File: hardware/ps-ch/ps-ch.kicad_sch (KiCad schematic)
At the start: 70 parts, among them Q11 MMBT3904, U10 ADuM1401xRW, U11 LMR51610X, U13 ADuM1401xRW, U3 LM61495, U5 OPA992IDBVR

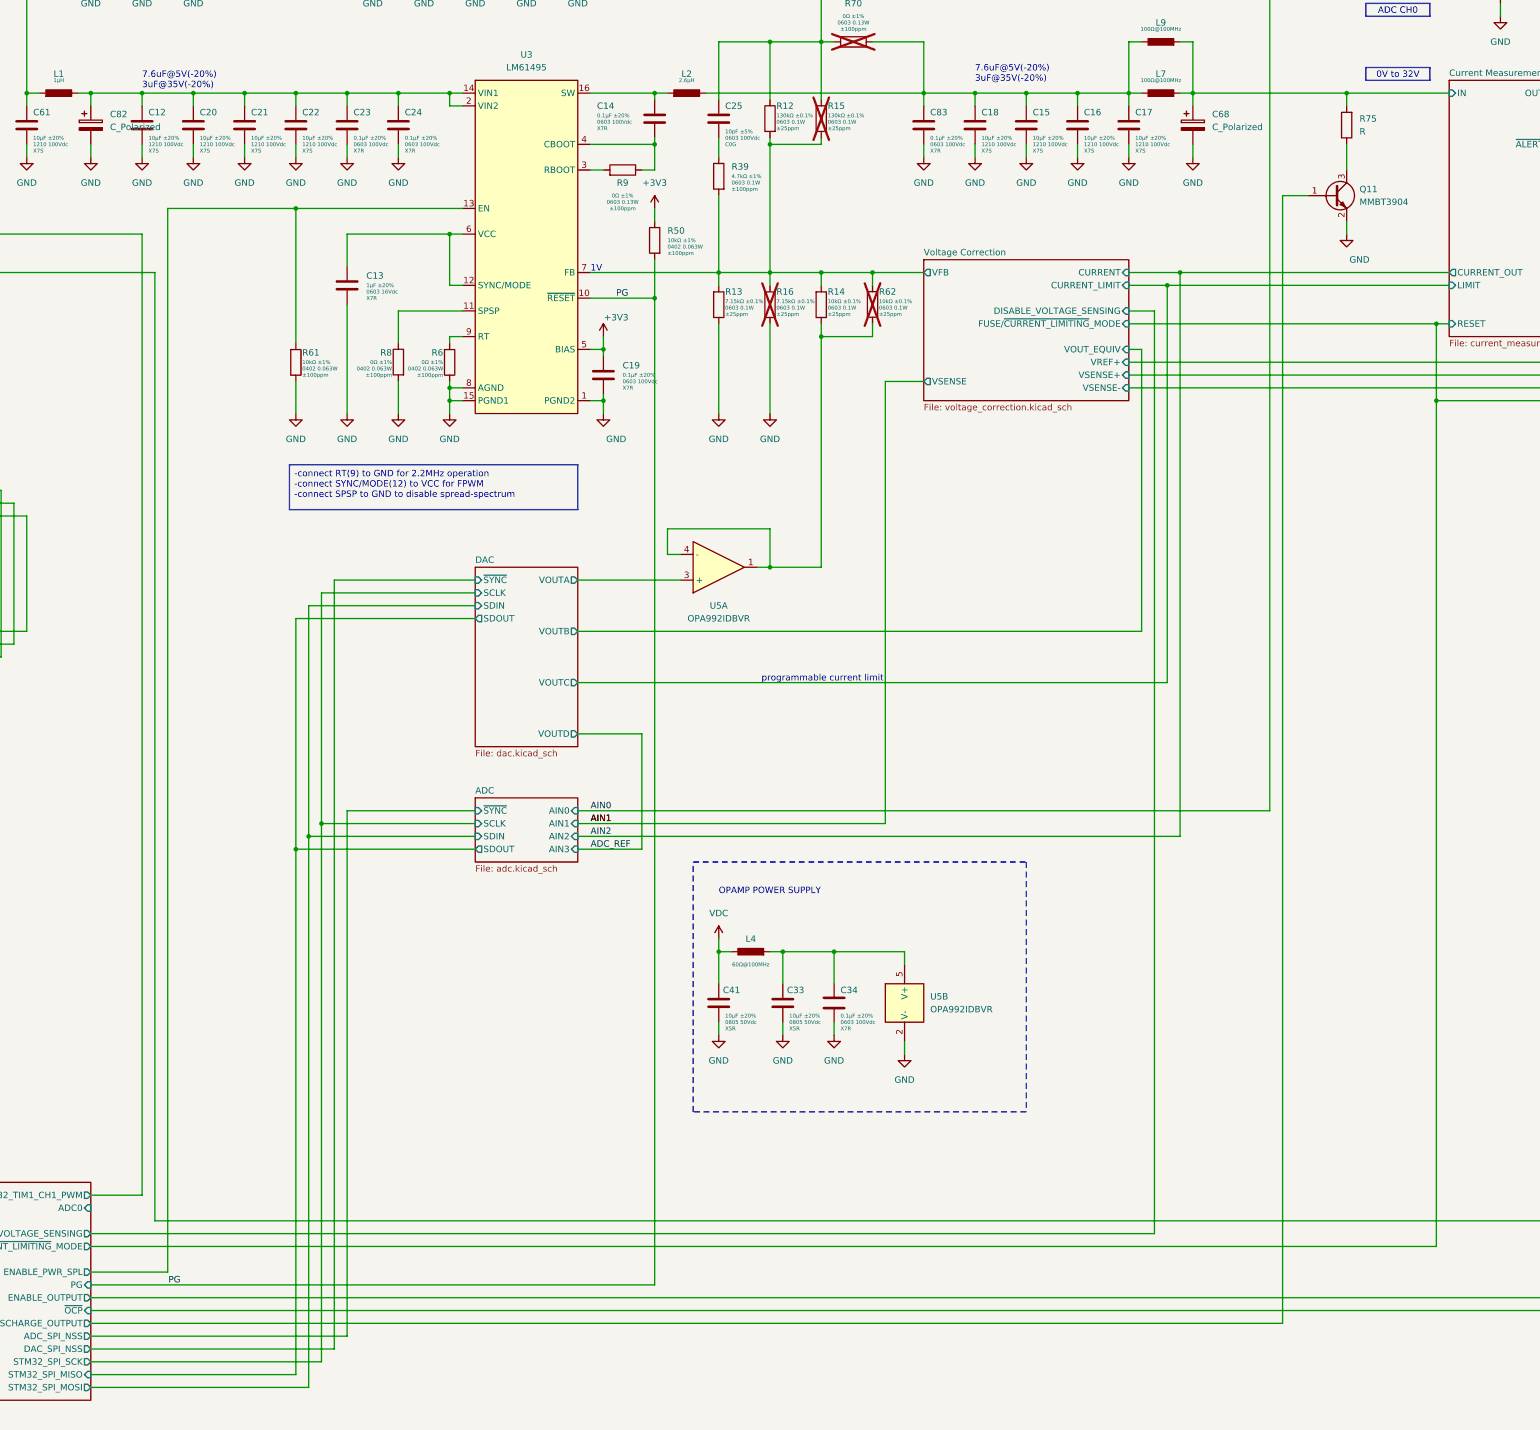
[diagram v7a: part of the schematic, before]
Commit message: added discharge resistors
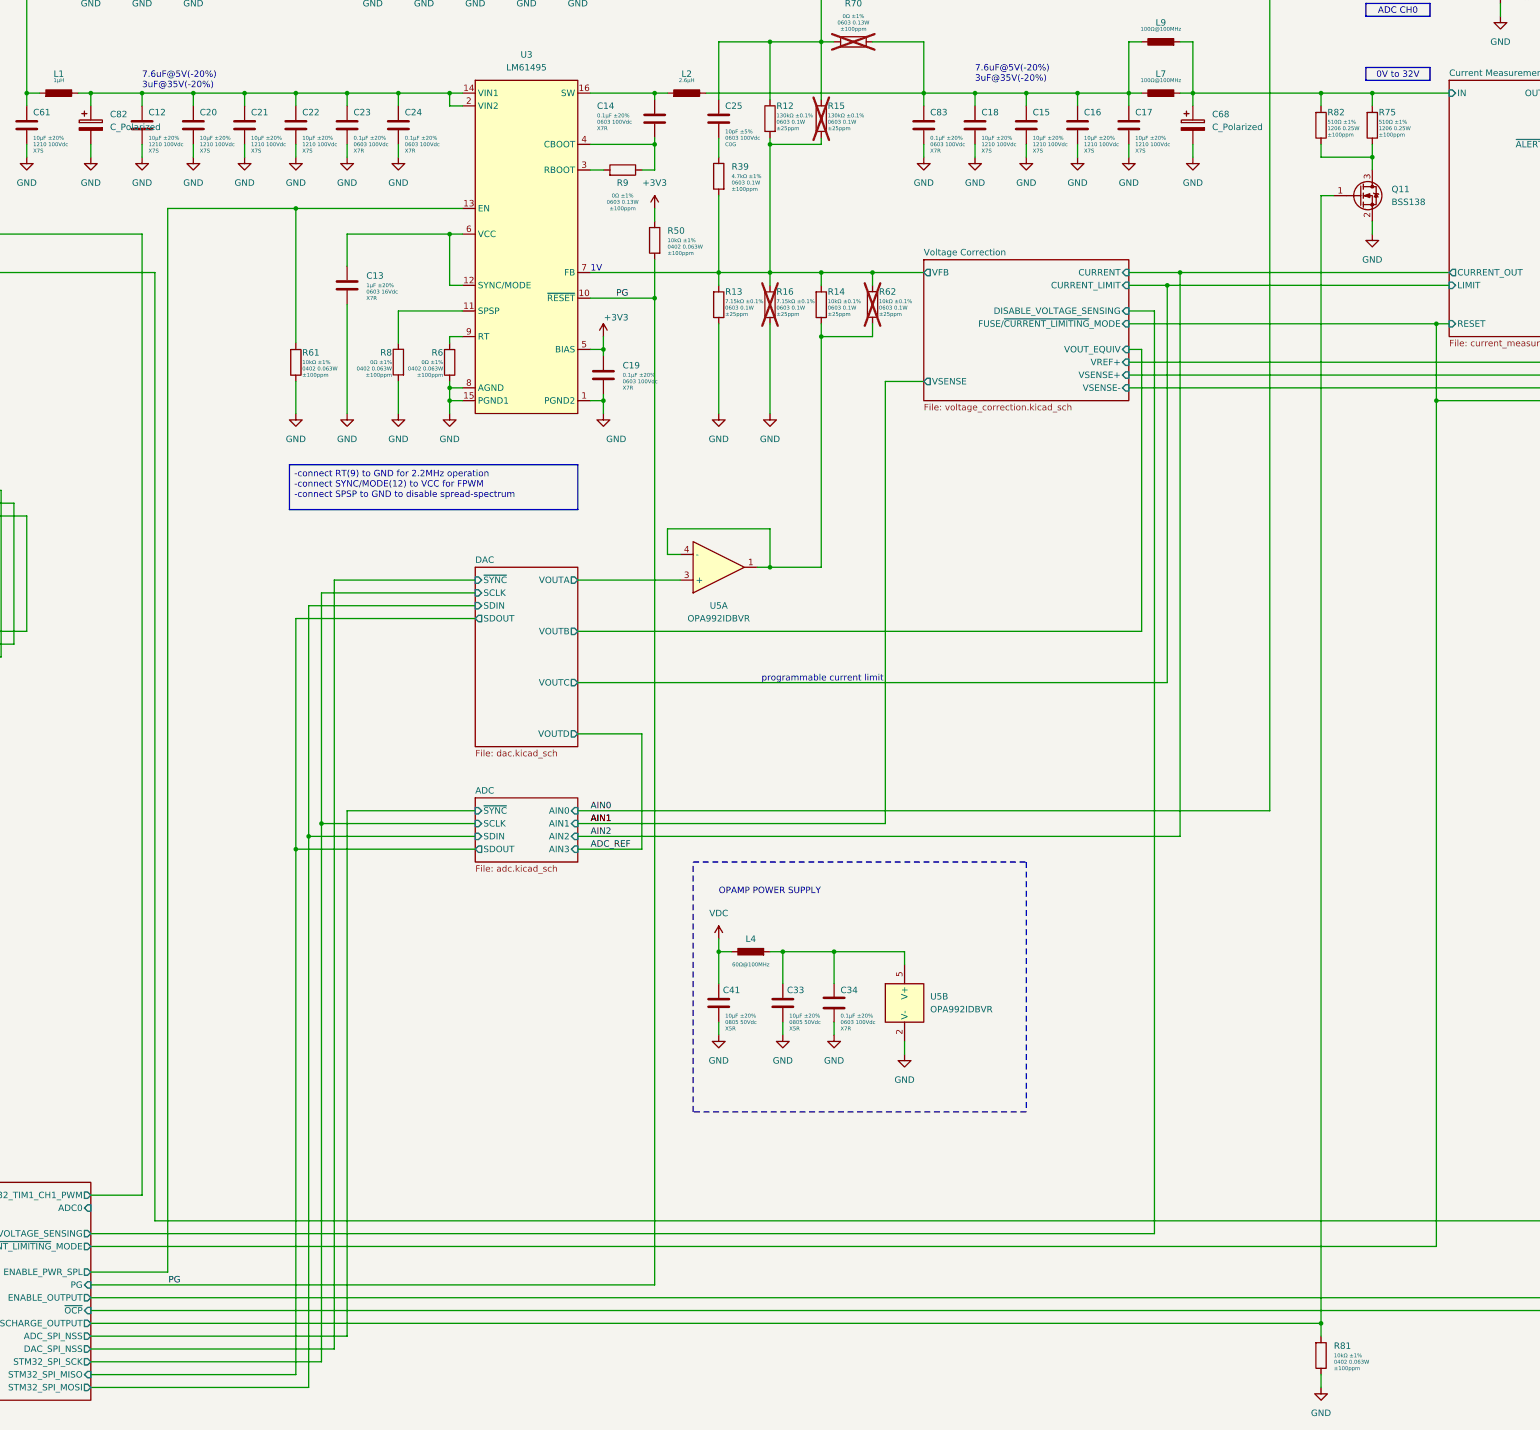
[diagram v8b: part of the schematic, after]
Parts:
- removed Q11: MMBT3904, Package_TO_SOT_SMD:SOT-23, symbol Transistor_BJT:MMBT3904
- removed R75: R, symbol Device:R
- added Q11: BSS138, Package_TO_SOT_SMD:SOT-23, symbol Transistor_FET:BSS138
- added R75, R82: 510Ω 1206 0.25W ±1% ±100ppm/°C, Resistor_SMD:R_1206_3216Metric, symbol ps-ch:500Ω 1206 0.25W ±1% ±100ppm/°C
- added R81: 10kΩ 0402 0.063W ±1% ±100ppm/°C, Resistor_SMD:R_0402_1005Metric, symbol ps-ch:10kΩ 0402 0.063W ±1% ±100ppm/°C
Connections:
- net Current Measurement/IN: now also R75.2, R82.2
- net GND: now also Q11.2 (S), R81.1
- net STM32/DISCHARGE_OUTPUT: now also Q11.1 (G), R81.2
- new net: Q11.3 (D), R75.1, R82.1
